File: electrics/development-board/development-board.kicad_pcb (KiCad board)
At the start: 2 copper layers, 153 x 77 mm, 103 parts, among them J1 East, J10 Ext_5V, J2 Screw_Terminal, J3 USB_B, J4 Keyboard, J5 Mouse, J6 Audio, J7 VGA, J8 West, J9 PinOut, Q1 MMBT3904, Q2 MMBT3904, Q3 S8050, Q4 S8050, SW1 Reset, SW2 Setup, SW3 Power, U1 LD1117S33, U2 FT2232HL, U3 93C46-WMN6TP, U4 LTV-817S, U5 LTV-817S, U6 MAX3486, U7 SN74CBT16292, U8 SN74CBT16292, Y1 12MHz

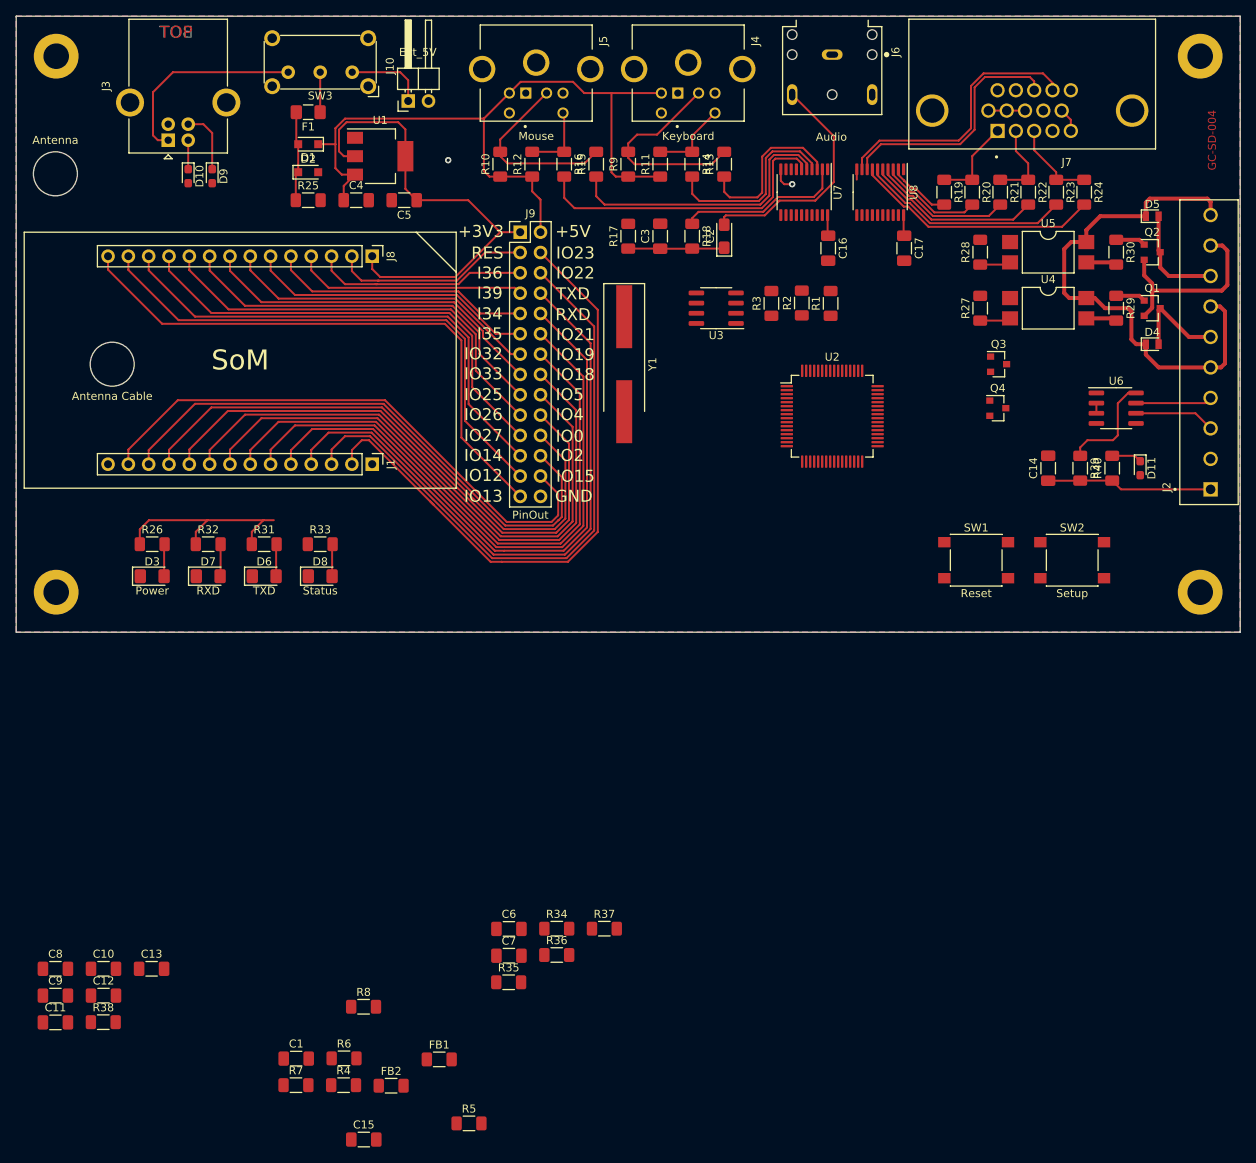
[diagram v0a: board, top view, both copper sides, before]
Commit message: INOA-372 Rename Fab and Dev board
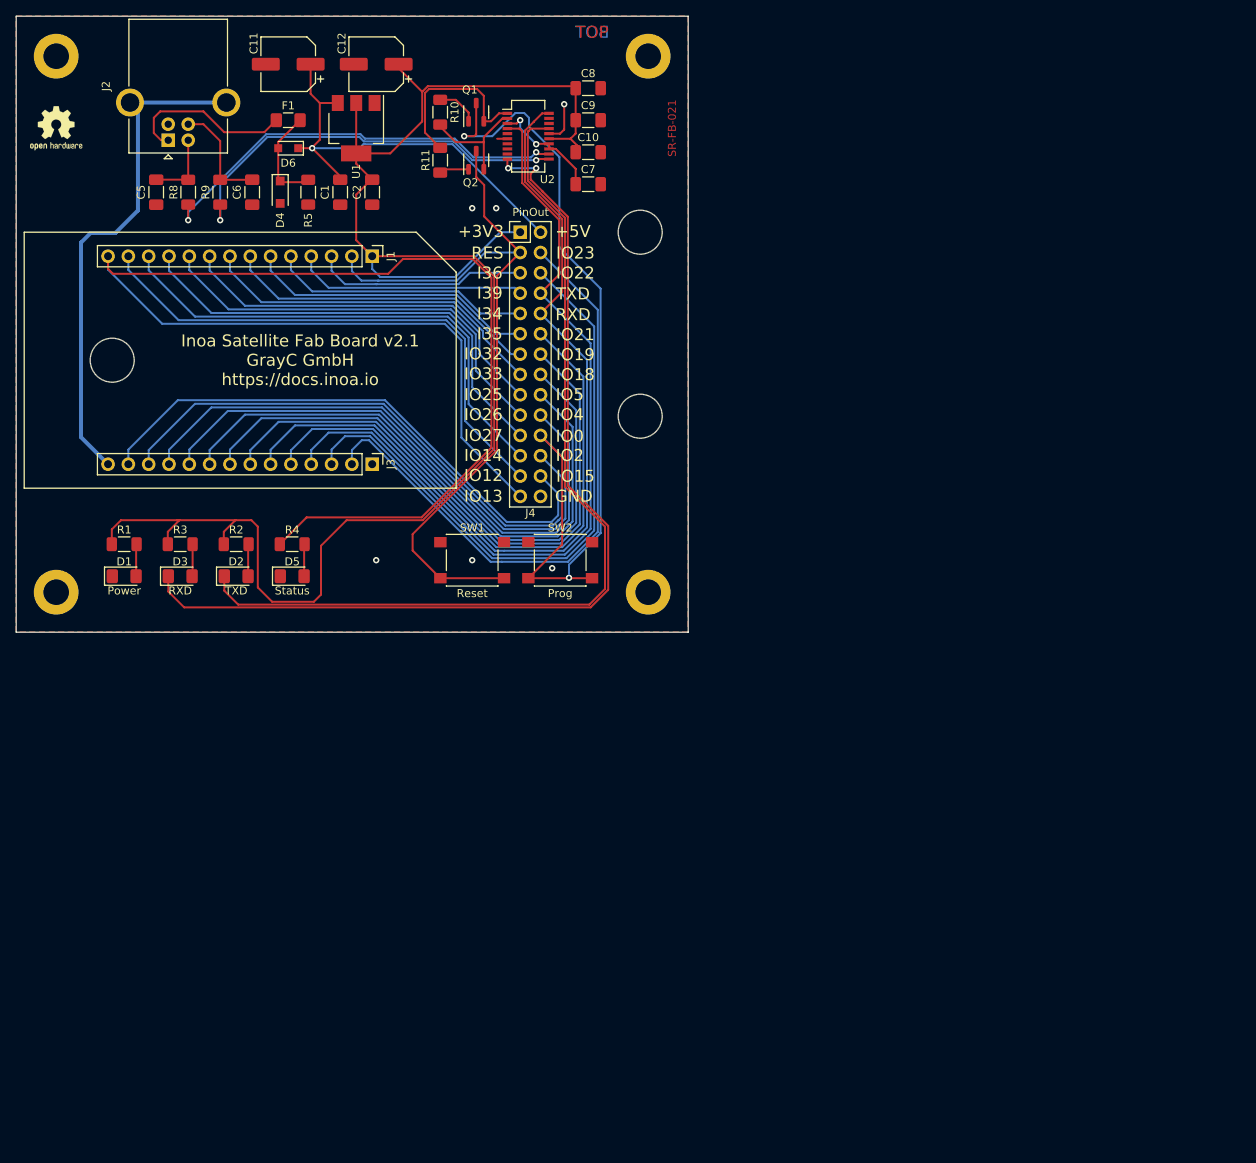
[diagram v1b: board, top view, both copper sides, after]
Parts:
- removed C13: 0u1, Capacitor_SMD:C_1206_3216Metric_Pad1.33x1.80mm_HandSolder
- removed C14, C15, C16, C17, C3: 100nF, Capacitor_SMD:C_1206_3216Metric_Pad1.33x1.80mm_HandSolder
- removed the C2 at (138.5, 77.5)
- removed D10, D11, D9: D_TVS, Diode_SMD:D_0603_1608Metric_Pad1.05x0.95mm_HandSolder
- removed the D4 at (192.0, 91.0)
- removed the D5 at (192.0, 75.0)
- removed FB1, FB2: 1k@100MHz, Resistor_SMD:R_1206_3216Metric_Pad1.30x1.75mm_HandSolder
- removed J10: Ext_5V, Connector_PinHeader_2.54mm:PinHeader_1x02_P2.54mm_Horizontal
- removed the J3 at (69.0, 65.5)
- removed the J4 at (134.0, 55.8)
- removed J5: Mouse, footprints:TE_5749180-1
- removed J6: Audio, footprints:CUI_SJ1-3523N
- removed J7: VGA, footprints:AMPHENOL_L77HDE15SD1CH4F
- removed the Q1 at (192.0, 86.5)
- removed the Q2 at (192.0, 79.5)
- removed the R10 at (110.5, 68.5)
- removed the R11 at (130.5, 68.5)
- removed R12: 2k, Resistor_SMD:R_1206_3216Metric_Pad1.30x1.75mm_HandSolder
- removed R13, R14, R15, R16: 120R, Resistor_SMD:R_1206_3216Metric_Pad1.30x1.75mm_HandSolder
- removed R17: 150R, Resistor_SMD:R_1206_3216Metric_Pad1.30x1.75mm_HandSolder
- removed R18: 270R, Resistor_SMD:R_1206_3216Metric_Pad1.30x1.75mm_HandSolder
- removed R19, R21, R23: 400R, Resistor_SMD:R_1206_3216Metric_Pad1.30x1.75mm_HandSolder
- removed R20, R22, R24: 800R, Resistor_SMD:R_1206_3216Metric_Pad1.30x1.75mm_HandSolder
- removed R27, R28, R29, R30: 220R, Resistor_SMD:R_1206_3216Metric_Pad1.30x1.75mm_HandSolder
- removed the R3 at (144.4, 85.9)
- removed R34, R35, R7: 10k, Resistor_SMD:R_1206_3216Metric_Pad1.30x1.75mm_HandSolder
- removed R38: 12k, Resistor_SMD:R_1206_3216Metric_Pad1.30x1.75mm_HandSolder
- removed R39, R40: R, Resistor_SMD:R_1206_3216Metric_Pad1.30x1.75mm_HandSolder
- removed the R4 at (90.9, 183.6)
- removed the R5 at (106.6, 188.4)
- removed R6: 2k2, Resistor_SMD:R_1206_3216Metric_Pad1.30x1.75mm_HandSolder
- removed the R8 at (93.4, 173.8)
- removed the R9 at (126.5, 68.5)
- removed SW3: Power, Button_Switch_THT:SW_E-Switch_EG1224_SPDT_Angled
- removed U3: 93C46-WMN6TP, Package_SO:SOIC-8_3.9x4.9mm_P1.27mm
- removed U4, U5: LTV-817S, Package_DIP:SMDIP-4_W9.53mm
- removed U6: MAX3486, Package_SO:SOIC-8_3.9x4.9mm_P1.27mm
- removed U7, U8: SN74CBT16292, Package_SO:TSSOP-20_4.4x6.5mm_P0.65mm
- removed Y1: 12MHz, Crystal:Crystal_SMD_HC49-SD_HandSoldering
- added G1: LOGO, images:grayc-logo-negative, F.Cu at (55.0, 72.0)
- added H4: Cable, MountingHole:MountingHole_5.5mm, F.Cu at (128.0, 100.0)
- added LOGO1: Logo_Open_Hardware_Small, Symbol:OSHW-Logo2_7.3x6mm_SilkScreen, F.Cu at (55.0, 64.0)
- C11: value 0u1 -> 100uF; footprint Capacitor_SMD:C_1206_3216Metric_Pad1.33x1.80mm_HandSolder -> Capacitor_SMD:CP_Elec_6.3x5.4
- C12: value 4u7 -> 47uF; footprint Capacitor_SMD:C_1206_3216Metric_Pad1.33x1.80mm_HandSolder -> Capacitor_SMD:CP_Elec_6.3x5.4
- C5: renamed from C1; value 100nF -> 47pF
- C6: value C -> 47pF
- C7: value C -> 100nF
- C8, C9: value 12pF -> 100nF
- D4: renamed from D1; value BZT52C6V2 -> MM3Z6V2T1G; footprint Diode_SMD:D_SOD-323_HandSoldering -> Diode_SMD:D_SOD-123F
- F1: value 6V/800mA -> 5V/1A
- H1: renamed from H5; value Antenna Cable -> Cable
- H2: renamed from H1; value MountingHole_Pad -> Stand
- H3: renamed from H2; value MountingHole_Pad -> Stand
- H5: renamed from H3; value MountingHole_Pad -> Stand
- H6: value Antenna -> Cable
- H7: renamed from H4; value MountingHole_Pad -> Stand
- J2: value Screw_Terminal -> USB; footprint footprints:TE_1-1776113-0 -> Connector_USB:USB_B_OST_USB-B1HSxx_Horizontal
- Q1: renamed from Q3; footprint Package_TO_SOT_SMD:SOT-23 -> Package_TO_SOT_SMD:SOT-23-3
- Q2: renamed from Q4; footprint Package_TO_SOT_SMD:SOT-23 -> Package_TO_SOT_SMD:SOT-23-3
- R8: renamed from R1; value 33R -> 27R
- R9: renamed from R2; value 33R -> 27R
- SW2: value Setup -> Prog
- U2: value FT2232HL -> FT231XS; footprint Package_QFP:LQFP-64_10x10mm_P0.5mm -> Package_SO:SSOP-20_3.9x8.7mm_P0.635mm
- moved J2 133.0 mm to (69.0, 65.5)
- moved C8 128.7 mm to (121.5, 59.0)
- moved C9 128.1 mm to (121.5, 63.0)
- moved C11 123.3 mm to (84.0, 56.0), turned to 180 degrees
- moved C12 121.3 mm to (95.0, 56.0), turned to 180 degrees
- moved C10 118.7 mm to (121.5, 67.0)
- moved C5 109.7 mm to (67.5, 72.0), turned to -90 degrees
- moved R10 106.4 mm to (103.0, 62.0), turned to -90 degrees
- moved R11 98.2 mm to (103.0, 68.0), turned to 90 degrees
- moved C6 97.5 mm to (79.5, 72.0), turned to -90 degrees
- moved C7 96.9 mm to (121.5, 71.0)
- moved R8 81.5 mm to (71.5, 72.0)
- moved R9 74.0 mm to (75.5, 72.0)
- moved H6 73.5 mm to (128.0, 77.0)
- moved Q1 72.5 mm to (107.5, 62.0), turned to 90 degrees
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- renumbered C4 to C1, C5 to C2, D3 to D1, D6 to D2, D7 to D3, D8 to D5, D2 to D6, J8 to J1, J1 to J3, J9 to J4, R26 to R1, R36 to R10, R37 to R11, R31 to R2, R32 to R3, R33 to R4, R25 to R5
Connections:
- C10 pad 1: Net-(C10-Pad1) -> +3V3
- C11 pad 1: Net-(C10-Pad1) -> +5V
- C12 pad 1: Net-(C12-Pad1) -> +3V3
- C5 pad 1: +3V3 -> D-
- C6 pad 1: Chip_PU -> D+
- C7 pad 1: IO0 -> Net-(C7-Pad1)
- C8 pad 1: Net-(C8-Pad1) -> +3V3
- C9 pad 1: Net-(C9-Pad1) -> +3V3
- D1 pad 2: Net-(D3-Pad2) -> Net-(D1-Pad2)
- D2 pad 2: Net-(D6-Pad2) -> Net-(D2-Pad2)
- D3 pad 2: Net-(D7-Pad2) -> Net-(D3-Pad2)
- D4 pad 1: Net-(D1-Pad1) -> Net-(D4-Pad1)
- D5 pad 2: Net-(D8-Pad2) -> Net-(D5-Pad2)
- D6 pad 2: Net-(D1-Pad1) -> Net-(D4-Pad1)
- F1 pad 2: Net-(D1-Pad1) -> Net-(D4-Pad1)
- J2 pad 1: S0 -> Net-(F1-Pad1)
- J2 pad 2: GND -> D-
- J2 pad 3: RS485_A -> D+
- J2 pad 4: RS485_B -> GND
- J2 pad 5: VS -> GND
- Q1 pad 1: FT_~{DTR} -> Net-(Q1-Pad1)
- Q1 pad 2: Net-(Q3-Pad2) -> FT_~{DTR}
- Q2 pad 1: FT_~{RTS} -> Net-(Q2-Pad1)
- Q2 pad 2: Net-(Q4-Pad2) -> FT_~{RTS}
- R1 pad 1: +3V3 -> Net-(D1-Pad2)
- R1 pad 2: Net-(D3-Pad2) -> +3V3
- R10 pad 1: Net-(Q3-Pad2) -> Net-(Q1-Pad1)
- R11 pad 1: FT_~{DTR} -> Net-(Q2-Pad1)
- R11 pad 2: Net-(Q4-Pad2) -> FT_~{DTR}
- R2 pad 1: +3V3 -> Net-(D2-Pad2)
- R2 pad 2: Net-(D6-Pad2) -> +3V3
- R3 pad 1: +3V3 -> Net-(D3-Pad2)
- R3 pad 2: Net-(D7-Pad2) -> +3V3
- R4 pad 1: IO13 -> Net-(D5-Pad2)
- R4 pad 2: Net-(D8-Pad2) -> IO13
- R5 pad 1: Net-(D1-Pad1) -> GND
- R5 pad 2: GND -> Net-(D4-Pad1)
- R8 pad 1: EECS -> Net-(R8-Pad1)
- R8 pad 2: Net-(R1-Pad2) -> D-
- R9 pad 1: EECLK -> Net-(R9-Pad1)
- R9 pad 2: Net-(R2-Pad2) -> D+
- U2 pad 1: GND -> FT_~{DTR}
- U2 pad 10: GND -> RX_LED
- U2 pad 11: GND -> Net-(R9-Pad1)
- U2 pad 12: Net-(U2-Pad12) -> Net-(R8-Pad1)
- U2 pad 13: GND -> Net-(C7-Pad1)
- U2 pad 14: Net-(U2-Pad14) -> Net-(C7-Pad1)
- U2 pad 15: GND -> +3V3
- U2 pad 16: FT_TCK -> GND
- U2 pad 17: FT_TDI -> TX_LED
- U2 pad 18: FT_TDO -> unconnected-(U2-Pad18)
- U2 pad 19: FT_TMS -> unconnected-(U2-Pad19)
- U2 pad 2: Net-(C8-Pad1) -> FT_~{RTS}
- U2 pad 20: Net-(U2-Pad20) -> U0RXD
- U2 pad 3: Net-(C9-Pad1) -> Net-(C7-Pad1)
- U2 pad 4: Net-(C10-Pad1) -> U0TXD
- U2 pad 5: GND -> unconnected-(U2-Pad5)
- U2 pad 6: Net-(R38-Pad1) -> GND
- U2 pad 7: USB_DN -> unconnected-(U2-Pad7)
- U2 pad 8: USB_DP -> unconnected-(U2-Pad8)
- U2 pad 9: Net-(C12-Pad1) -> unconnected-(U2-Pad9)
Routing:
- net RX_LED: track 0.00 -> 120.3 mm, vias 0 -> 2
- net TX_LED: track 0.00 -> 114.9 mm
- net IO0: track 72.1 -> 178.7 mm, vias 0 -> 2
- net +3V3: track 103.1 -> 209.3 mm
- net IO13: track 72.1 -> 176.2 mm
- net Chip_PU: track 24.9 -> 95.6 mm
- net VS: track 65.6 -> 0.00 mm
- net GND: track 11.9 -> 70.4 mm, vias 2 -> 6
- net Net-(R8-Pad1): track 0.00 -> 53.6 mm, vias 0 -> 2
- net Net-(R9-Pad1): track 0.00 -> 51.3 mm, vias 0 -> 2
- net +5V: track 94.0 -> 54.0 mm, vias 0 -> 1
- net PS2_1_Data: track 39.1 -> 0.00 mm
- net PS2_1_Clock: track 35.6 -> 0.00 mm
- net VSync: track 34.1 -> 0.00 mm
- net Blue_Low: track 31.0 -> 0.00 mm
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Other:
- board size 153 x 77 mm -> 84 x 77 mm
- board text added: "Inoa Satellite Fab Board v2.1 GrayC GmbH https://docs.inoa.io"
- board text added: "SR-FB-021"
- board text removed: "GC-SD-004"
- board text removed: "SoM"
